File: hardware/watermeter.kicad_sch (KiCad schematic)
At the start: 52 parts, among them J1 Screw_Terminal_01x03, J10 SRD-05VDC-SL-C, J11 SRD-05VDC-SL-C, J2 Screw_Terminal_01x03, J3 Conn_01x08_Pin, J4 Conn_01x08_Pin, J5 TC2030, J7 USB-TYPE-C-31-M-12, J8 Screw_Terminal_01x02, J9 Screw_Terminal_01x02, K1 SRD-05VDC-SL-C, K2 SRD-05VDC-SL-C, Q1 PDTD123YK, Q2 PDTD123YK, SW1 Reboot, U3 ESP32-C6-MINI-1, U4 USBLC6-2SC6

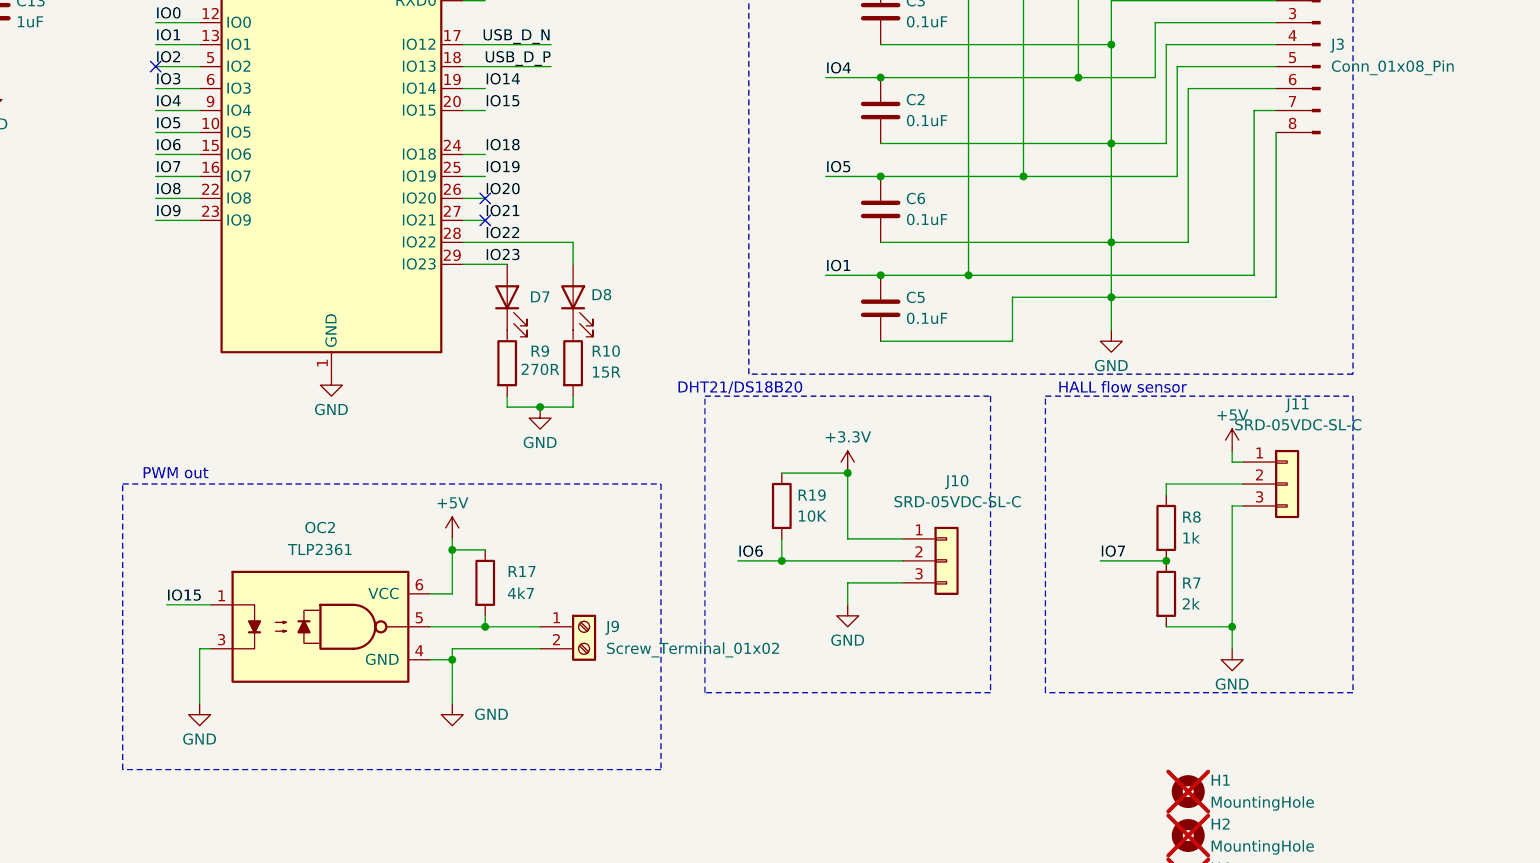
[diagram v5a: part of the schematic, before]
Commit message: Production - V2 Added: TagConnect port for fast firmware upload Fixes: Resistive diider fo hall sensor was replaced with transistor logic Refactoring for whole power supply Minimal track width 0.2mm Fixed digital transistor pin swap
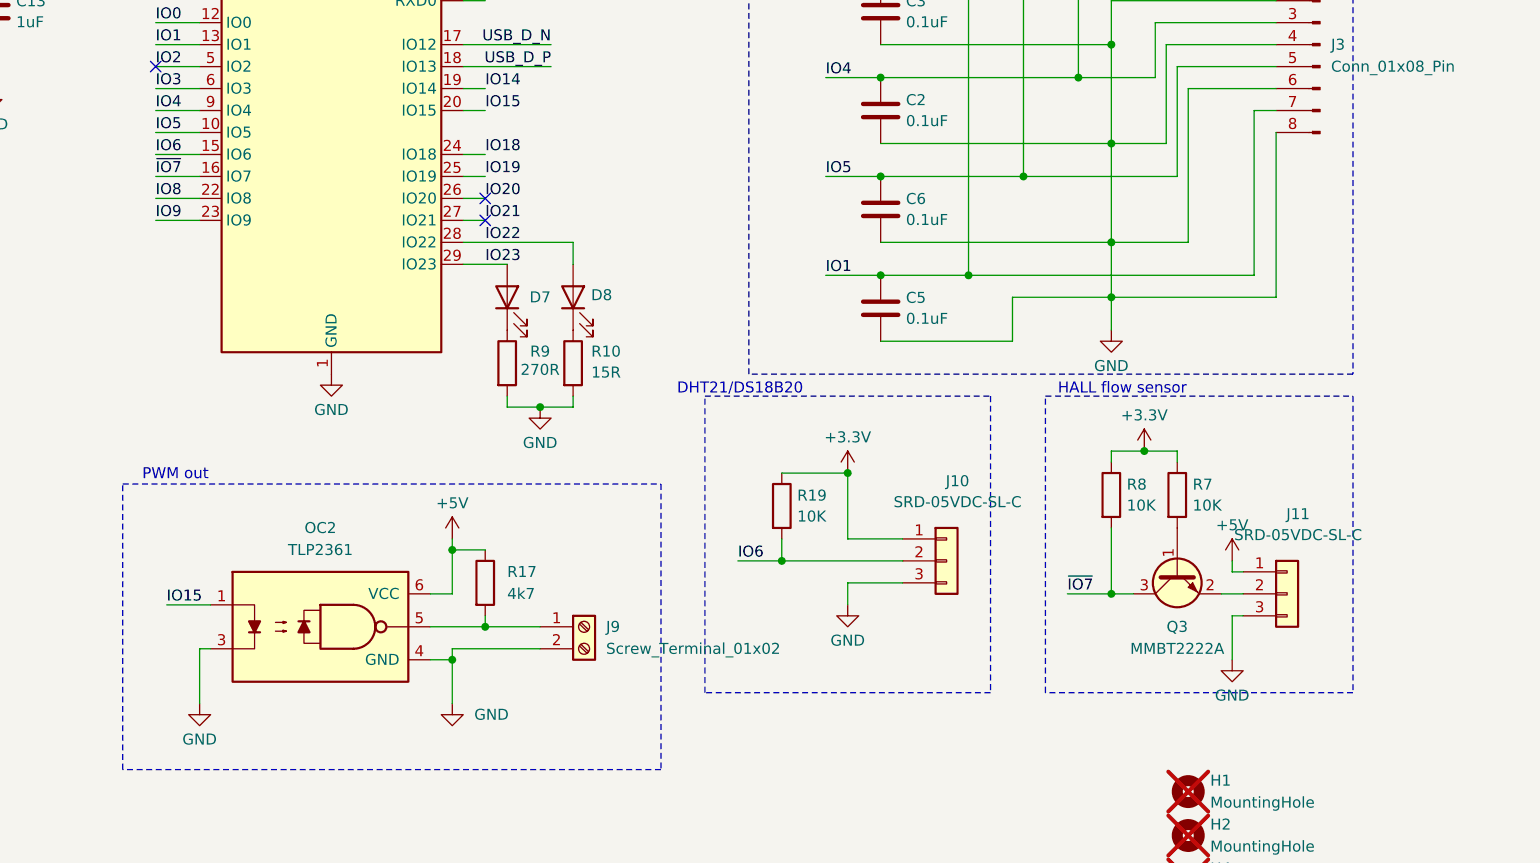
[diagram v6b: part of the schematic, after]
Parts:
- added Q3: MMBT2222A, PCM_Package_TO_SOT_SMD_AKL:SOT-23, symbol PCM_Transistor_BJT_AKL:MMBT2222A
- R7: value 2k -> 10K; LCSC Part # C17604 -> C17414
- R8: value 1k -> 10K; LCSC Part # C17513 -> C17414
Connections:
- net +3.3V: now also R7.1, R8.1
- net GND: no longer R7.2
- net at J11.2 (Pin_2): now also Q3.2 (E); no longer R8.1
- net IO7 renamed ~{IO7}
- net ~{IO7}: now also Q3.3 (C); no longer R7.1
- new net: Q3.1 (B), R7.2
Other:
- moved on the sheet: J11
